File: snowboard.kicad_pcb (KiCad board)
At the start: 4 copper layers, 62.8 x 35.5 mm, 37 parts, among them J1 Micro USB Port, J2 B2B-PH-K-S, Q1 S8050, Q2 S8050, SW1 BOOT, SW2 RESET, U1 ESP32-WROVER-E-N4R8, U2 CP2102N-A02-GQFN28R, U3 SPX3819M5-L-3-3, U4 MCP73831T-2ACI_OT, U5 MPU-6050

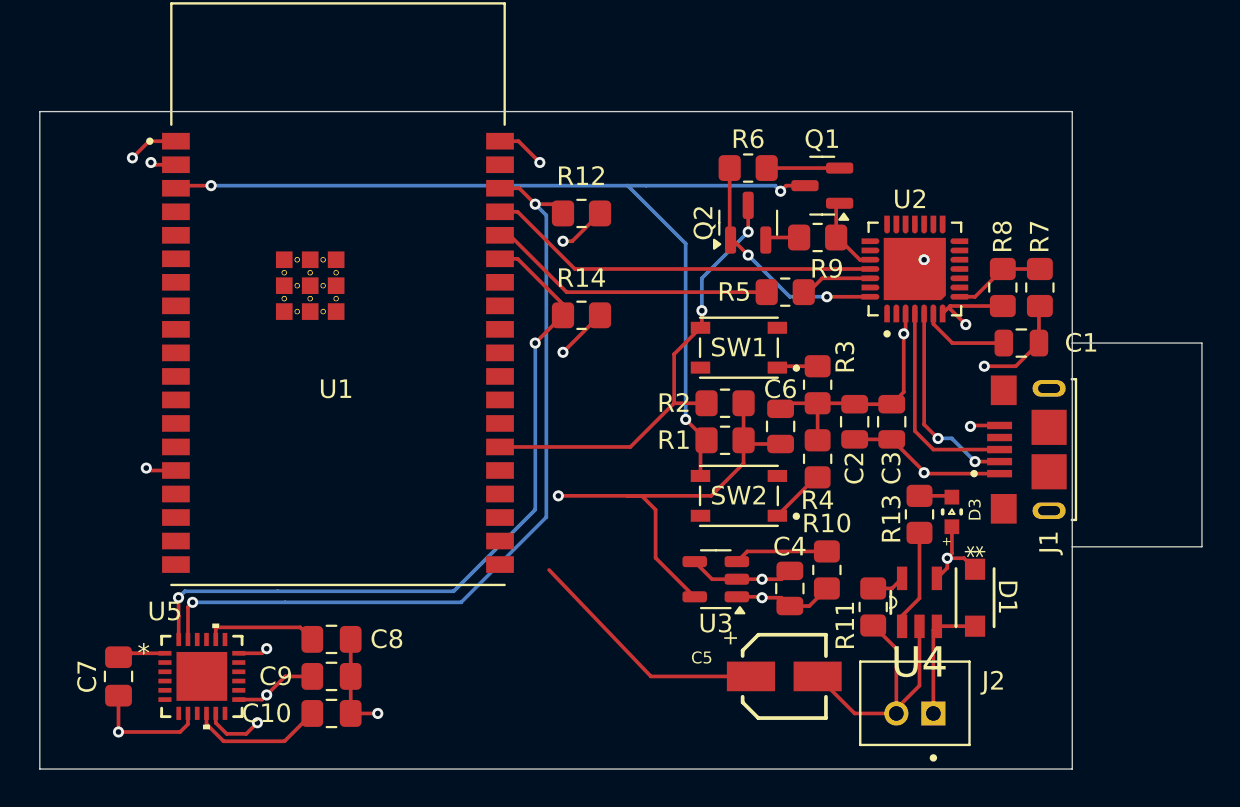
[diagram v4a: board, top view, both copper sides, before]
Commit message: Add test points
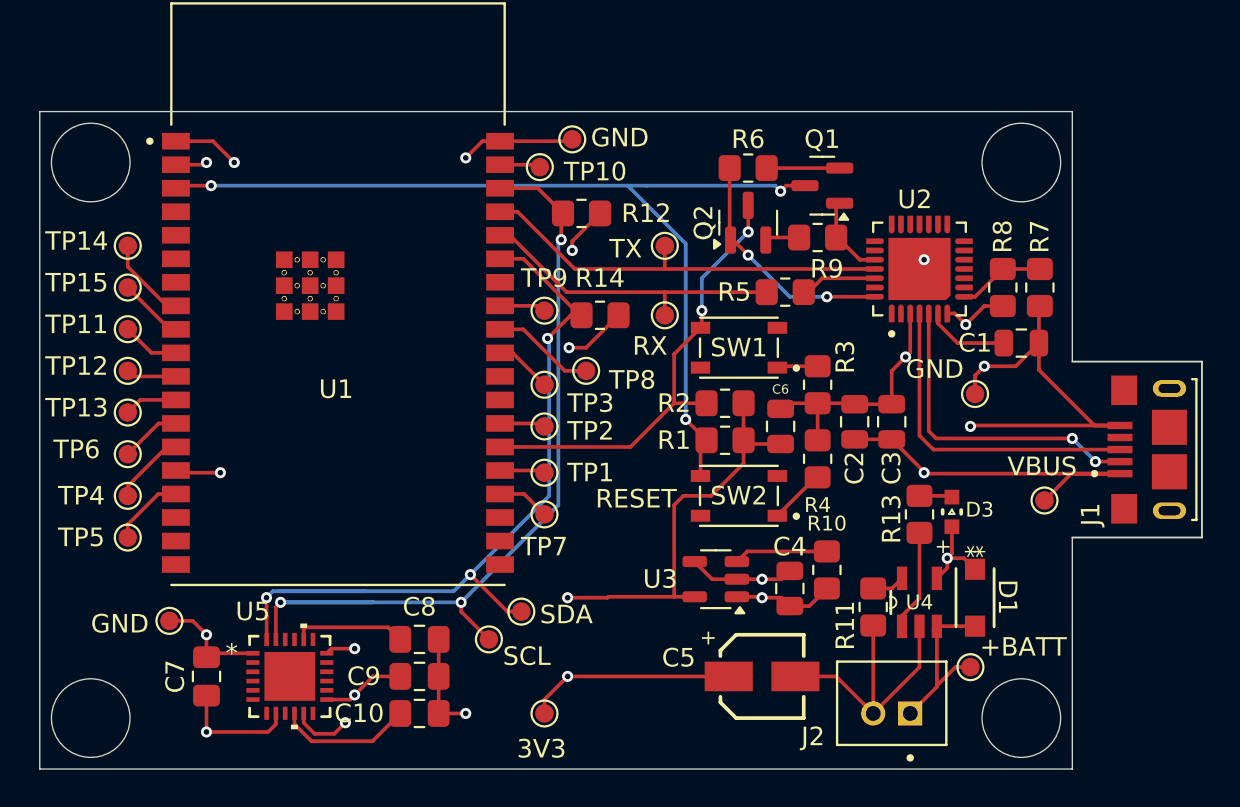
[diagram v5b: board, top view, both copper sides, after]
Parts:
- added TP1: TestPoint, TestPoint:TestPoint_Pad_D1.0mm, F.Cu at (157.0, 128.5)
- added TP10: TestPoint, TestPoint:TestPoint_Pad_D1.0mm, F.Cu at (156.8, 112.0)
- added TP11: TestPoint, TestPoint:TestPoint_Pad_D1.0mm, F.Cu at (134.5, 120.8)
- added TP12: TestPoint, TestPoint:TestPoint_Pad_D1.0mm, F.Cu at (134.5, 123.0)
- added TP13: TestPoint, TestPoint:TestPoint_Pad_D1.0mm, F.Cu at (134.5, 125.2)
- added TP14: TestPoint, TestPoint:TestPoint_Pad_D1.0mm, F.Cu at (134.5, 116.2)
- added TP15: TestPoint, TestPoint:TestPoint_Pad_D1.0mm, F.Cu at (134.5, 118.5)
- added TP16: TestPoint, TestPoint:TestPoint_Pad_D1.0mm, F.Cu at (154.0, 137.5)
- added TP17: TestPoint, TestPoint:TestPoint_Pad_D1.0mm, F.Cu at (155.8, 136.0)
- added TP18: TestPoint, TestPoint:TestPoint_Pad_D1.0mm, F.Cu at (180.0, 139.0)
- added TP19: TestPoint, TestPoint:TestPoint_Pad_D1.0mm, F.Cu at (180.2, 124.2)
- added TP2: TestPoint, TestPoint:TestPoint_Pad_D1.0mm, F.Cu at (157.0, 126.0)
- added TP20: TestPoint, TestPoint:TestPoint_Pad_D1.0mm, F.Cu at (157.0, 141.5)
- added TP21: TestPoint, TestPoint:TestPoint_Pad_D1.0mm, F.Cu at (158.5, 110.5)
- added TP22: TestPoint, TestPoint:TestPoint_Pad_D1.0mm, F.Cu at (184.0, 130.0)
- added TP23: TestPoint, TestPoint:TestPoint_Pad_D1.0mm, F.Cu at (136.8, 136.5)
- added TP24: TestPoint, TestPoint:TestPoint_Pad_D1.0mm, F.Cu at (163.5, 120.0)
- added TP25: TestPoint, TestPoint:TestPoint_Pad_D1.0mm, F.Cu at (163.5, 116.2)
- added TP3: TestPoint, TestPoint:TestPoint_Pad_D1.0mm, F.Cu at (157.0, 123.8)
- added TP4: TestPoint, TestPoint:TestPoint_Pad_D1.0mm, F.Cu at (134.5, 129.8)
- added TP5: TestPoint, TestPoint:TestPoint_Pad_D1.0mm, F.Cu at (134.5, 132.0)
- added TP6: TestPoint, TestPoint:TestPoint_Pad_D1.0mm, F.Cu at (134.5, 127.5)
- added TP7: TestPoint, TestPoint:TestPoint_Pad_D1.0mm, F.Cu at (157.0, 130.8)
- added TP8: TestPoint, TestPoint:TestPoint_Pad_D1.0mm, F.Cu at (159.2, 123.0)
- added TP9: TestPoint, TestPoint:TestPoint_Pad_D1.0mm, F.Cu at (157.0, 119.8)
- moved J1 6.50 mm to (190.8, 127.2)
- moved C10 4.75 mm to (150.2, 141.5)
- moved C7 4.75 mm to (138.8, 139.5)
- moved C8 4.75 mm to (150.2, 137.5)
- moved C9 4.75 mm to (150.2, 139.5)
- moved U5 4.75 mm to (143.2, 139.5)
- moved J2 1.25 mm to (175.8, 140.9)
- moved C5 1.20 mm to (168.8, 139.5)
- moved R14 1.00 mm to (160.0, 120.0)
- moved U2 0.25 mm to (177.2, 117.5)
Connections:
- U1 pad 10: unconnected-(U1-IO25-Pad10) -> Net-(U1-IO25)
- U1 pad 11: unconnected-(U1-IO26-Pad11) -> Net-(U1-IO26)
- U1 pad 12: unconnected-(U1-IO27-Pad12) -> Net-(U1-IO27)
- U1 pad 13: unconnected-(U1-IO14-Pad13) -> Net-(U1-IO14)
- U1 pad 14: unconnected-(U1-IO12-Pad14) -> Net-(U1-IO12)
- U1 pad 16: unconnected-(U1-IO13-Pad16) -> Net-(U1-IO13)
- U1 pad 23: unconnected-(U1-IO15-Pad23) -> Net-(U1-IO15)
- U1 pad 24: unconnected-(U1-IO2-Pad24) -> Net-(U1-IO2)
- U1 pad 26: unconnected-(U1-IO4-Pad26) -> Net-(U1-IO4)
- U1 pad 29: unconnected-(U1-IO5-Pad29) -> Net-(U1-IO5)
- U1 pad 30: unconnected-(U1-IO18-Pad30) -> Net-(U1-IO18)
- U1 pad 31: unconnected-(U1-IO19-Pad31) -> Net-(U1-IO19)
- U1 pad 37: unconnected-(U1-IO23-Pad37) -> Net-(U1-IO23)
- U1 pad 8: unconnected-(U1-IO32-Pad8) -> Net-(U1-IO32)
- U1 pad 9: unconnected-(U1-IO33-Pad9) -> Net-(U1-IO33)
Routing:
- net GND: track 61.2 -> 86.4 mm, vias 11 -> 12
- net VBUS: track 23.9 -> 34.2 mm
- net /D_P: track 11.3 -> 18.0 mm
- net /D_N: track 11.0 -> 17.6 mm
- net Net-(U1-IO18): track 0.00 -> 5.58 mm
- net /I2C_SDA: track 39.6 -> 44.7 mm, vias 2 -> 3
- net Net-(U1-IO32): track 0.00 -> 4.60 mm
- net Net-(U1-IO12): track 0.00 -> 4.00 mm
- net Net-(U1-IO13): track 0.00 -> 3.98 mm
- net Net-(U1-IO33): track 0.00 -> 3.54 mm
- net Net-(U1-IO14): track 0.00 -> 3.29 mm
- net +BATT: track 6.60 -> 9.86 mm
- net Net-(U1-IO25): track 0.00 -> 3.13 mm
- net Net-(U1-IO5): track 0.00 -> 3.11 mm
- net Net-(U1-IO27): track 0.00 -> 2.88 mm
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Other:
- outline, holes or cut-outs redrawn
- board text added: "+BATT"
- board text added: "3V3"
- board text added: "GND"
- board text added: "RESET"
- board text added: "RX"
- board text added: "SCL"
- board text added: "SDA"
- board text added: "TX"
- board text added: "VBUS"

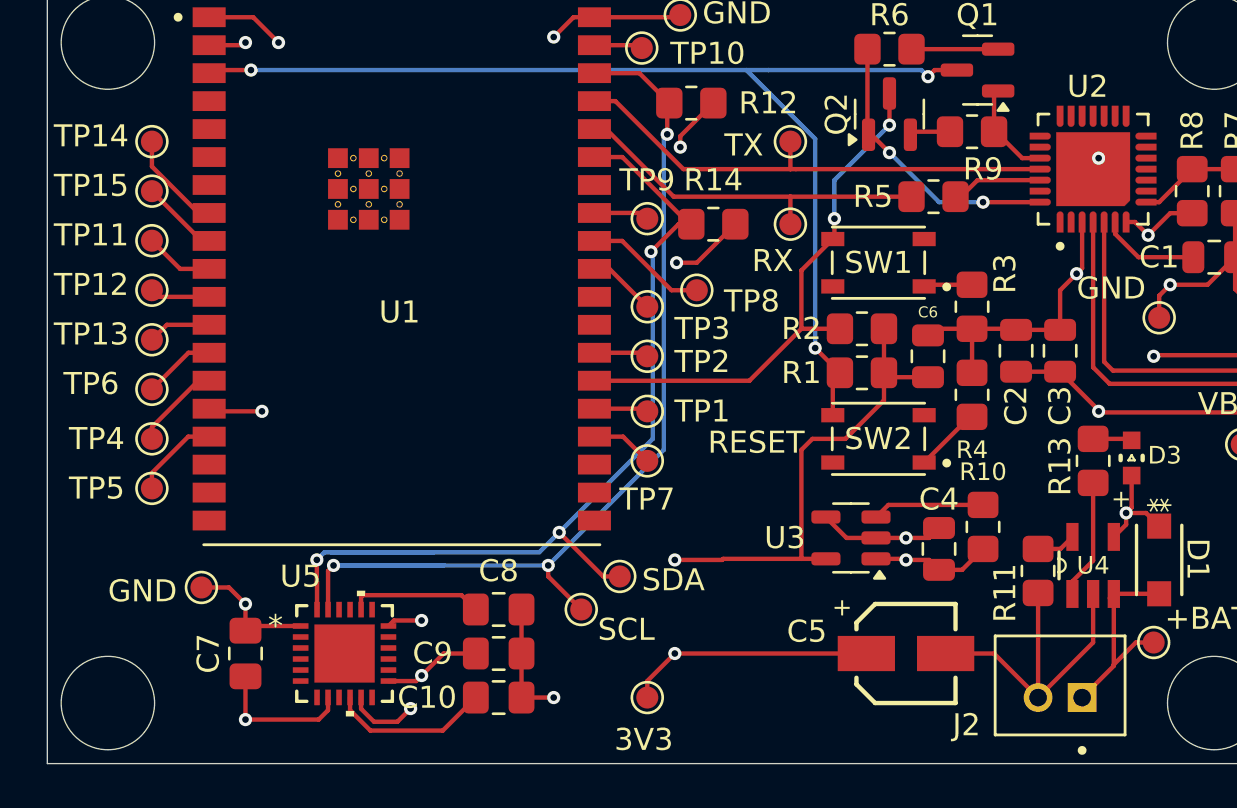
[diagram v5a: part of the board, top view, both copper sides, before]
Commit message: Swap discontinued MPU6050 for BNO086
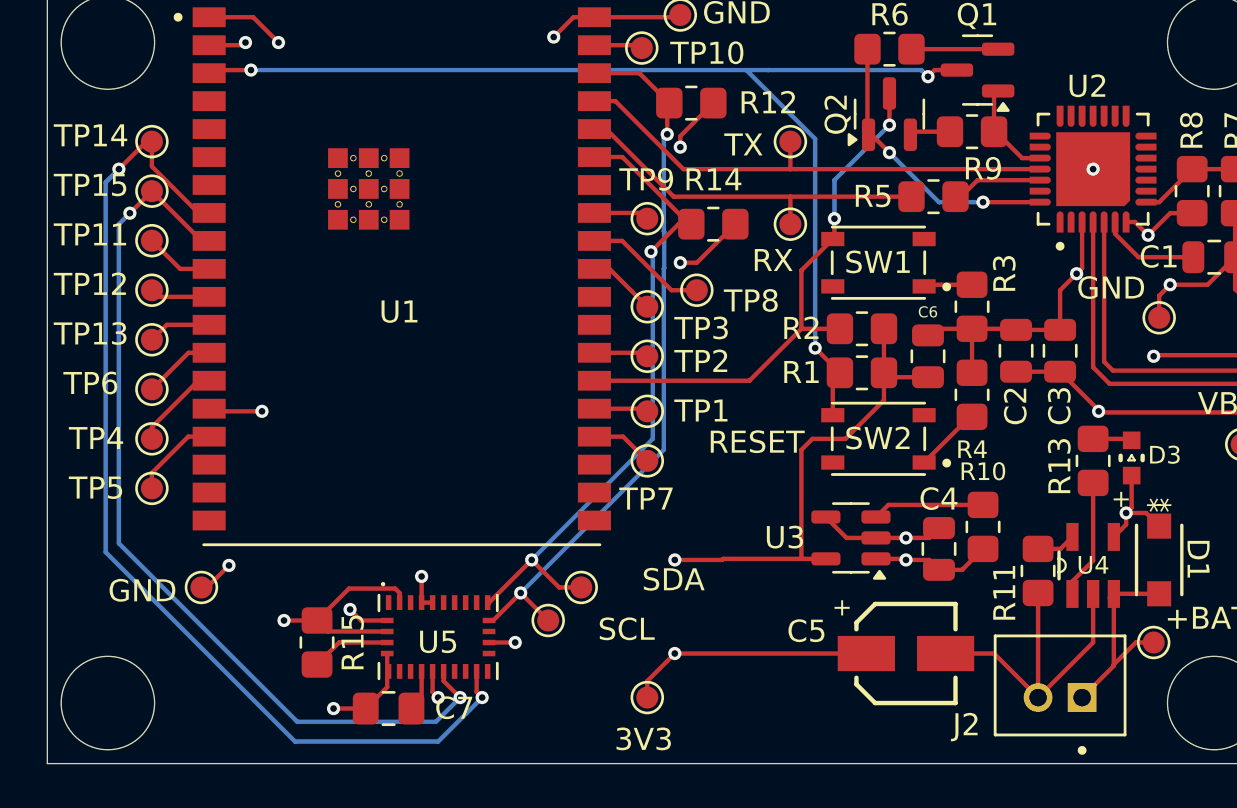
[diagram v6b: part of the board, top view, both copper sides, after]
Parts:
- removed C10: 0.1uF, Capacitor_SMD:C_0805_2012Metric_Pad1.18x1.45mm_HandSolder
- removed C8: 2.2nF, Capacitor_SMD:C_0805_2012Metric_Pad1.18x1.45mm_HandSolder
- removed C9: 10nF, Capacitor_SMD:C_0805_2012Metric_Pad1.18x1.45mm_HandSolder
- added R15: 10k, Resistor_SMD:R_0805_2012Metric_Pad1.20x1.40mm_HandSolder, F.Cu at (142.0, 139.0)
- U5: value MPU-6050 -> BNO080; footprint USER_FP:MPU6050_QFN24_4X4X0P9-0P5_TDK -> USER_FP:IC_BNO080
- moved C7 6.96 mm to (145.2, 142.0), turned to 0 degrees
- moved U5 4.32 mm to (147.5, 138.8)
- moved TP17 1.82 mm to (154.0, 136.5)
- moved TP16 1.58 mm to (152.5, 138.0)
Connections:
- C7 pad 1: +3.3V -> GND
- C7 pad 2: GND -> Net-(U5-CAP)
- TP14 pad 1: Net-(U1-IO32) -> /BNO_HINTN
- TP15 pad 1: Net-(U1-IO33) -> /BNO_NRST
- U1 pad 8: Net-(U1-IO32) -> /BNO_HINTN
- U1 pad 9: Net-(U1-IO33) -> /BNO_NRST
- U5 pad 1: GND -> (no net)
- U5 pad 10: Net-(U5-REGOUT) -> +3.3V
- U5 pad 11: GND -> /BNO_NRST
- U5 pad 12: unconnected-(U5-INT-Pad12) -> (no net)
- U5 pad 13: +3.3V -> (no net)
- U5 pad 14: unconnected-(U5-NC-Pad14) -> /BNO_HINTN
- U5 pad 17: unconnected-(U5-NC-Pad17) -> GND
- U5 pad 18: GND -> unconnected-(U5-~{H_CS}-Pad18)
- U5 pad 19: unconnected-(U5-RESV-Pad19) -> /I2C_SCL
- U5 pad 2: unconnected-(U5-NC-Pad2) -> GND
- U5 pad 20: Net-(U5-CPOUT) -> /I2C_SDA
- U5 pad 21: unconnected-(U5-RESV-Pad21) -> (no net)
- U5 pad 22: unconnected-(U5-RESV-Pad22) -> (no net)
- U5 pad 23: /I2C_SCL -> (no net)
- U5 pad 24: /I2C_SDA -> (no net)
- U5 pad 25: unconnected-(U5-EPAD-Pad25) -> GND
- U5 pad 3: unconnected-(U5-NC-Pad3) -> +3.3V
- U5 pad 4: unconnected-(U5-NC-Pad4) -> Net-(U5-~{BOOT})
- U5 pad 5: unconnected-(U5-NC-Pad5) -> GND
- U5 pad 6: unconnected-(U5-AUX_DA-Pad6) -> GND
- U5 pad 7: unconnected-(U5-AUX_CL-Pad7) -> (no net)
- U5 pad 8: +3.3V -> (no net)
- U5 pad 9: unconnected-(U5-AD0-Pad9) -> Net-(U5-CAP)
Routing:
- net /BNO_HINTN: track 0.00 -> 47.1 mm, vias 0 -> 2
- net /BNO_NRST: track 0.00 -> 41.0 mm, vias 0 -> 2
- net /I2C_SDA: track 44.7 -> 30.0 mm, vias 3 -> 2
- net /I2C_SCL: track 46.5 -> 32.7 mm, vias 3 -> 2
- net Net-(U5-REGOUT): track 7.30 -> 0.00 mm
- net Net-(U5-CPOUT): track 6.09 -> 0.00 mm
- net GND: track 86.4 -> 80.8 mm, vias 12 -> 13
- net Net-(U1-IO32): track 4.60 -> 0.00 mm
- net Net-(U5-~{BOOT}): track 0.00 -> 3.60 mm
- net Net-(U1-IO33): track 3.54 -> 0.00 mm
- net Net-(U5-CAP): track 0.00 -> 1.88 mm

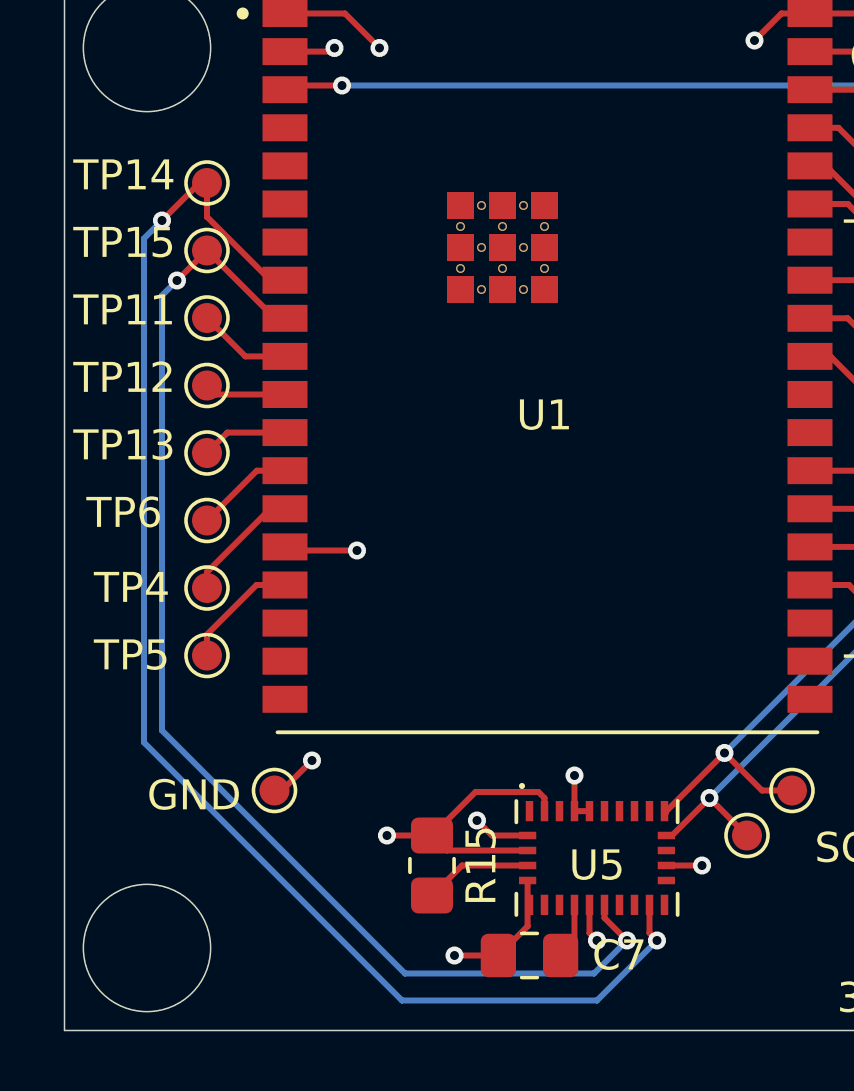
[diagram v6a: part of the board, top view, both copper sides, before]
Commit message: Fix track spacing
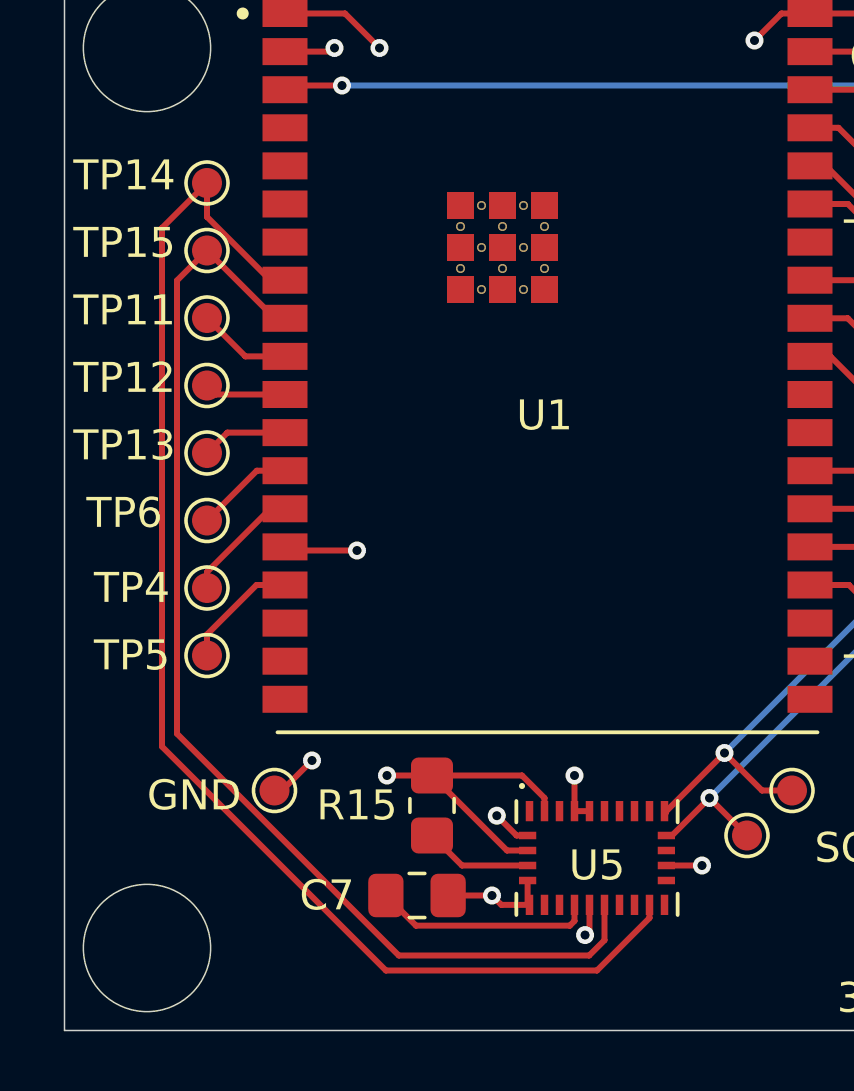
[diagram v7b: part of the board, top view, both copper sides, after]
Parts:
- moved C7 4.25 mm to (141.5, 140.0), turned to 180 degrees
- moved R15 2.00 mm to (142.0, 137.0)
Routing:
- net Net-(U5-CAP): track 1.88 -> 7.31 mm
- net /BNO_HINTN: track 47.1 -> 44.5 mm, vias 2 -> 0
- net /BNO_NRST: track 41.0 -> 38.8 mm, vias 2 -> 0
- net GND: track 80.8 -> 79.9 mm

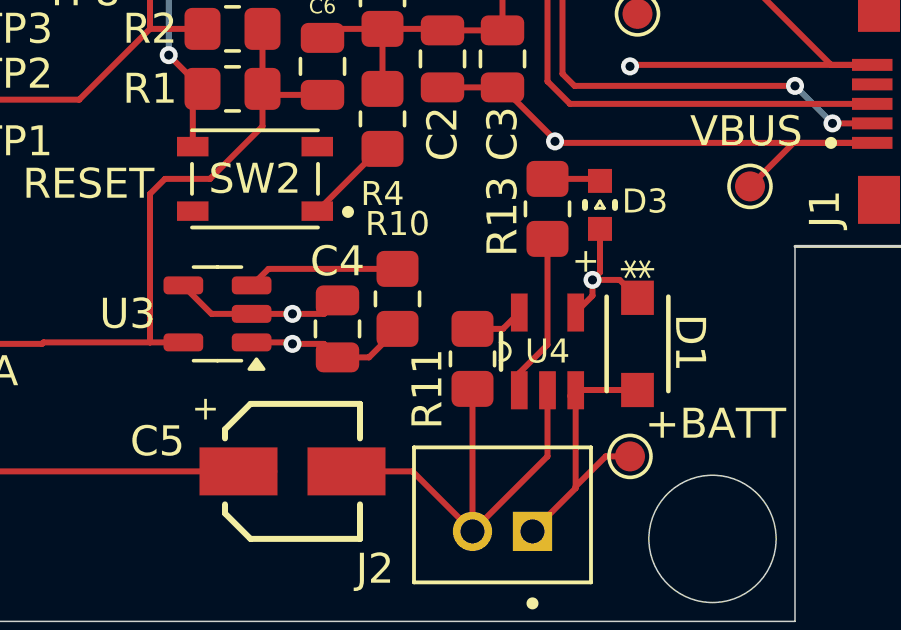
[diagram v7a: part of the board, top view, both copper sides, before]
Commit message: Reduce i2c pull-up value, fix shorting LDO, DNP auto-reset
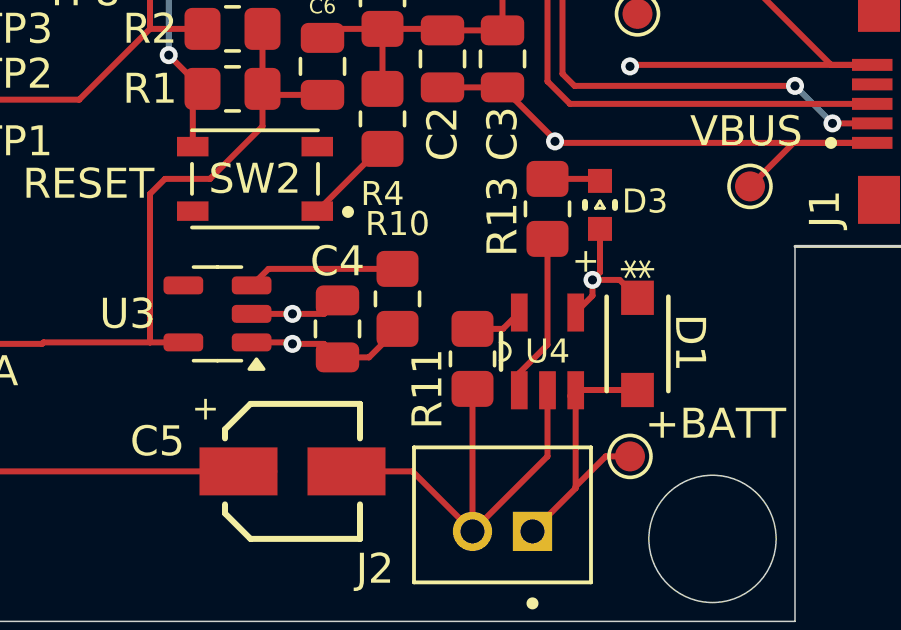
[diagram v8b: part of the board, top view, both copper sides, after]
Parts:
- R12, R14: value 100k -> 5k
- U5: value BNO080 -> BNO086
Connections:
- U3 pad 4: GND -> unconnected-(U3-BP-Pad4)
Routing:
- net GND: track 79.9 -> 77.3 mm
